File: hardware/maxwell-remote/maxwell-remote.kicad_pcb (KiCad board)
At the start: 2 copper layers, 77.5 x 38.1 mm, 46 parts, among them J1 INPUT, J2 UART, J3 Left, J4 Right, J5 Programmer, J6 B0_JMP, J7 B1_JMP, J8 SPI2, J9 ESP_BM, Q2 NDS332P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

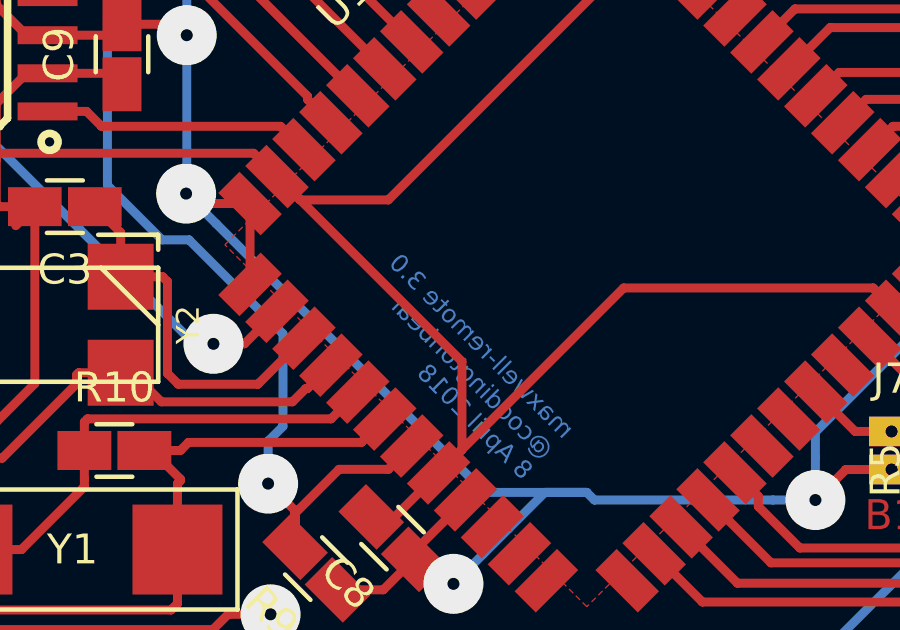
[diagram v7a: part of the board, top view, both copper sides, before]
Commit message: Updating pcb text.
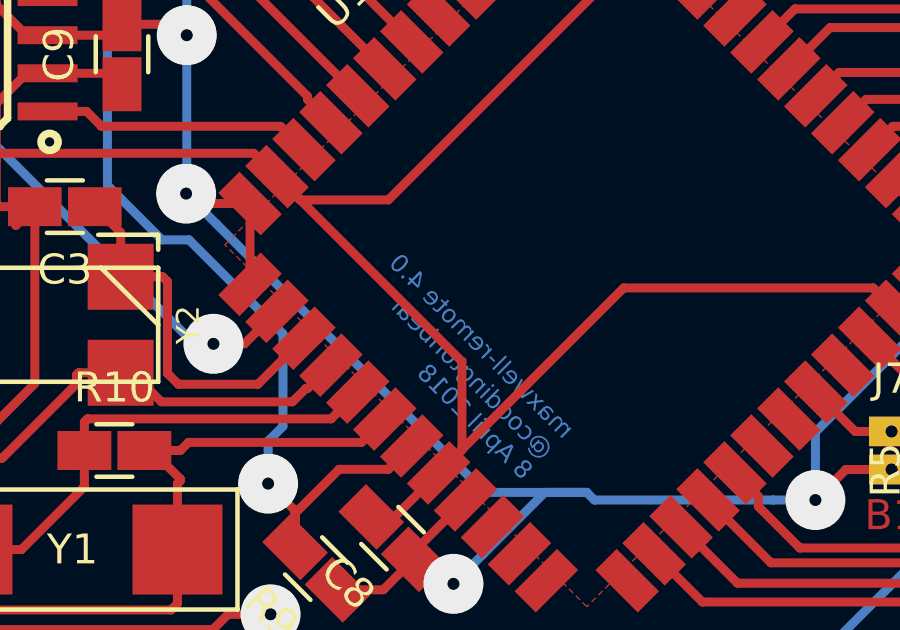
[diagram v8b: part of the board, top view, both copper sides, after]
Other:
- board text added: "maxwell-remote 4.0 @coddingtonbear 8 April 2018"
- board text removed: "maxwell-remote 3.0 @coddingtonbear 8 April 2018"
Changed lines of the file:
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@@
-(kicad_pcb (version 20171130) (host pcbnew "(2017-12-14 revision 75b21d0)-master")
+(kicad_pcb (version 20171130) (host pcbnew no-vcs-found-fddd5ab~61~ubuntu16.04.1)
   (general
     (thickness 1.6)
@@
       (viasonmask false)
       (mode 1)
-      (useauxorigin false)
+      (useauxorigin true)
       (hpglpennumber 1)
       (hpglpenspeed 20)
@@
     (effects (font (size 1 1) (thickness 0.25)) (justify mirror))
   )
-  (gr_text "maxwell-remote 3.0\n@coddingtonbear\n8 April 2018" (at 130.175 87.63 -45) (layer B.Cu)
+  (gr_text "maxwell-remote 4.0\n@coddingtonbear\n8 April 2018" (at 130.175 87.63 -45) (layer B.Cu)
     (effects (font (size 0.6 0.6) (thickness 0.125)) (justify left mirror))
   )
